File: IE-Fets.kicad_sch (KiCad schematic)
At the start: 12 parts, among them Q1 YJG150N03A, Q4 YJG150N03A, U4 INA185A1

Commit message: push for 8/8 order
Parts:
- removed C7: 4.7nF, Capacitor_SMD:C_0402_1005Metric, symbol Device:C
- removed D1: Z3V3, Diode_SMD:D_SOD-323_HandSoldering, symbol Device:D_Zener
- removed R1: 1mR, Resistor_SMD:R_1206_3216Metric, symbol Device:R
- removed R10: 15K, Resistor_SMD:R_0402_1005Metric, symbol Device:R
- removed R13: 2K2, Resistor_SMD:R_0402_1005Metric, symbol Device:R
- removed R16: 100R, Resistor_SMD:R_0402_1005Metric, symbol Device:R
- removed U4: INA185A1, Package_TO_SOT_SMD:SOT-563, symbol AlfredoSymbols:INA185A
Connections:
- net VCC is gone; now on net VFET: C1.1

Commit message: first push for v2
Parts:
- removed Q1, Q4: YJG150N03A, Package_TO_SOT_SMD:LFPAK56, symbol AlfredoSymbols:YJG150N03A
- added Q10: ~, AlfredoFootprints:PQFN8L, symbol AlfredoSymbols:HYG090ND06LS1C2
- C1: value 4.7uF,50V -> 4.7uF, 50V
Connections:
- net GND: now also Q10.1 (S1)
- net SHx: now also Q10.3 (S2), Q10.6 (D1)
- net VFET: now also Q10.5 (D2)
- net at R19.1: now also Q10.4 (G2)
- net at R21.1: now also Q10.2 (G1)
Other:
- moved on the sheet: R19, R21

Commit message: big schematic push for stm32g474
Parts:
- removed Q10: ~, AlfredoFootprints:PQFN8L, symbol AlfredoSymbols:HYG090ND06LS1C2
- removed R19, R21: 10R, Resistor_SMD:R_0402_1005Metric, symbol Device:R
- added D1: Z3V3, Diode_SMD:D_SOD-523, symbol Device:D_Zener
- added Q4: ~, AlfredoFootprints:DFN-8-2EP_6x5mm, symbol AlfredoSymbols:SE3082G
- added R11, R12: 10R, Resistor_SMD:R_0402_1005Metric, symbol Device:R
- added R13: 2mR, Resistor_SMD:R_1206_3216Metric, symbol Device:R
- added R14: 22K, Resistor_SMD:R_0402_1005Metric, symbol Device:R
- added R15, R16, R18: 2K2, Resistor_SMD:R_0402_1005Metric, symbol Device:R
- added R17: 15K, Resistor_SMD:R_0402_1005Metric, symbol Device:R
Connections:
- net GHx: now also R11.2
- net GLx: now also R12.2
- net GND: now also D1.2 (A), R13.2, R15.2, R18.1
- net SHx: now also Q4.5 (D2S1), R17.2
- net VFET: now also Q4.6 (D1)
- new net: Q4.2 (G1), R11.1
- new net: Q4.3 (S2), R13.1, R14.2, R15.1, R16.1
- new net: Q4.4 (G2), R12.1
- new net +3V3: R14.1
- new net sCURx+: R16.2
- new net sVLTx: D1.1 (K), R17.1, R18.2
- no-connect marks 0 -> 1

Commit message: cleaned up all files, created schematic PDF
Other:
- note removed: "gate resitors can be as low as 3.6 ohms?"
- note removed: "xESC uses 2.2uF,50V?"
- company: (none) -> AlfredoSystems
- title: (none) -> I3ESC

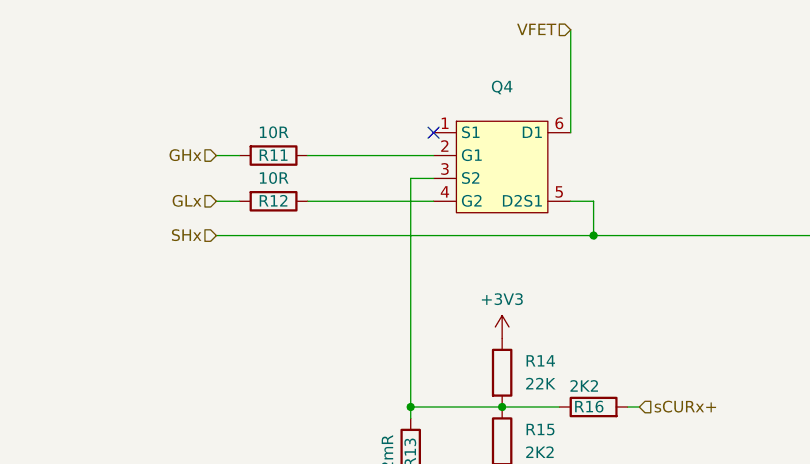
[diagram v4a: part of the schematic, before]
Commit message: Refactor net naming and update component values
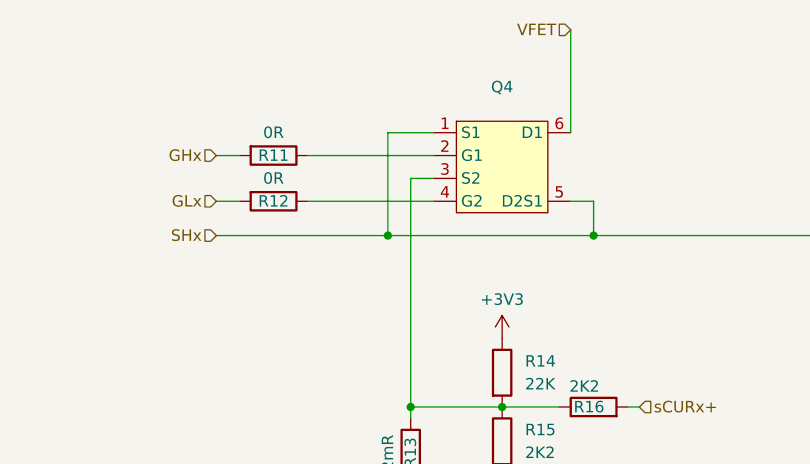
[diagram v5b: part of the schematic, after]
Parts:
- R11, R12: value 10R -> 0R; LCSC C25077 -> C17168
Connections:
- net SHx: now also Q4.1 (S1)
- no-connect marks 1 -> 0
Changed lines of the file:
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@@
+	)
+	(junction
+		(at 160.02 90.17)
+		(diameter 0)
+		(color 0 0 0 0)
 	)
 	(junction
@@
 		(color 0 0 0 0)
 	)
-	(no_connect
-		(at 165.1 78.74)
-	)
 	(wire
 		(pts
@@
 	(wire
 		(pts
+			(xy 160.02 78.74) (xy 160.02 90.17)
+		)
+		(stroke
+			(width 0)
+			(type default)
+		)
+	)
+	(wire
+		(pts
 			(xy 162.56 118.11) (xy 162.56 123.19)
 		)
@@
 	(wire
 		(pts
-			(xy 140.97 90.17) (xy 182.88 90.17)
+			(xy 140.97 90.17) (xy 160.02 90.17)
 		)
 		(stroke
@@
 	(wire
 		(pts
+			(xy 160.02 90.17) (xy 182.88 90.17)
+		)
+		(stroke
+			(width 0)
+			(type default)
+		)
+	)
+	(wire
+		(pts
 			(xy 217.17 113.03) (xy 217.17 115.57)
 		)
@@
 		(pts
 			(xy 172.72 109.22) (xy 179.07 109.22)
+		)
+		(stroke
+			(width 0)
+			(type default)
+		)
+	)
+	(wire
+		(pts
+			(xy 165.1 78.74) (xy 160.02 78.74)
 		)
 		(stroke
@@
 			)
 		)
-		(property "Value" "10R"
+		(property "Value" "0R"
 			(at 147.32 78.74 90)
 			(effects
@@
 			)
 		)
-		(property "Datasheet" "https://lcsc.com/product-detail/Chip-Resistor-Surface-Mount_UNI-ROYAL-Uniroyal-Elec-0402WGF100JTCE_C25077.html"
+		(property "Datasheet" "https://www.lcsc.com/product-detail/Chip-Resistor---Surface-Mount_UNI-ROYALUniroyal-Elec-UNI-ROYALUniroyal-Elec-0402WGF0000TCE_C17168.html"
 			(at 147.32 81.28 0)
 			(effects
@@
 			)
 		)
-		(property "LCSC" "C25077"
+		(property "LCSC" "C17168"
 			(at 147.32 81.28 0)
 			(effects
@@
 			)
 		)
-		(property "Value" "10R"
+		(property "Value" "0R"
 			(at 147.32 83.82 90)
 			(effects
@@
 			)
 		)
-		(property "Datasheet" "https://lcsc.com/product-detail/Chip-Resistor-Surface-Mount_UNI-ROYAL-Uniroyal-Elec-0402WGF100JTCE_C25077.html"
+		(property "Datasheet" "https://www.lcsc.com/product-detail/Chip-Resistor---Surface-Mount_UNI-ROYALUniroyal-Elec-UNI-ROYALUniroyal-Elec-0402WGF0000TCE_C17168.html"
 			(at 147.32 86.36 0)
 			(effects
@@
 			)
 		)
-		(property "LCSC" "C25077"
+		(property "LCSC" "C17168"
 			(at 147.32 86.36 0)
 			(effects

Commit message: Add decoupling capacitor to PG10 and update footprints
Added C17 (100nF, 50V) capacitor to PG10 for improved decoupling. Updated several footprint and property fields, fixed layer and sheetname attributes, and made minor net and pad stack changes for consistency with KiCAD 9.0. Updated LCSC part number for JST SH connector.
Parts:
- D1: LCSC C2891760 -> C131795
